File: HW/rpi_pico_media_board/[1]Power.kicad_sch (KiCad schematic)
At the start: 30 parts, among them IC1 LS1205EVD33, Q1 T2N7002AK, U3 HT7533-1

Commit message: Scheme improvements
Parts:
- renumbered C1 to C100, C2 to C101, C3 to C102, C4 to C103, C5 to C104, C6 to C105, C7 to C106, C8 to C107, C9 to C108, C10 to C109, C11 to C110, D1 to D100, D2 to D101, IC1 to IC100, J1 to J100, L1 to L100, PS1 to PS100, Q1 to Q100, R1 to R100, R2 to R101, R3 to R102, R4 to R103, R6 to R104, R5 to R105, R7 to R106, R8 to R107, R11 to R108, R9 to R109, R10 to R110, U3 to U100
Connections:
- net GND: now also IC100.11 (GND)
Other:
- moved on the sheet: D101, Q100, R109, R110

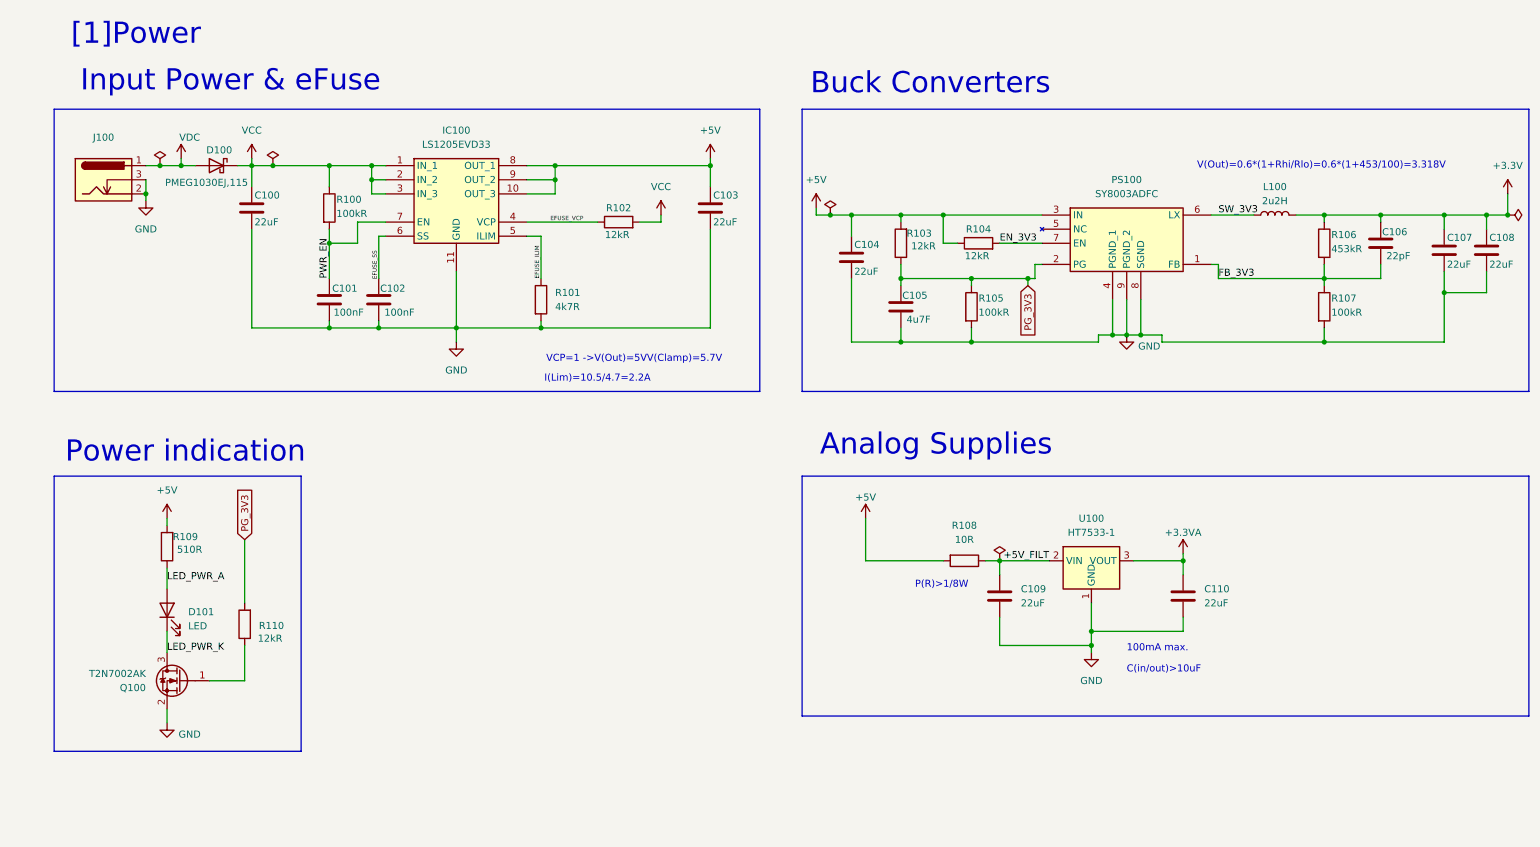
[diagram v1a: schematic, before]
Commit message: Minor BOM updates
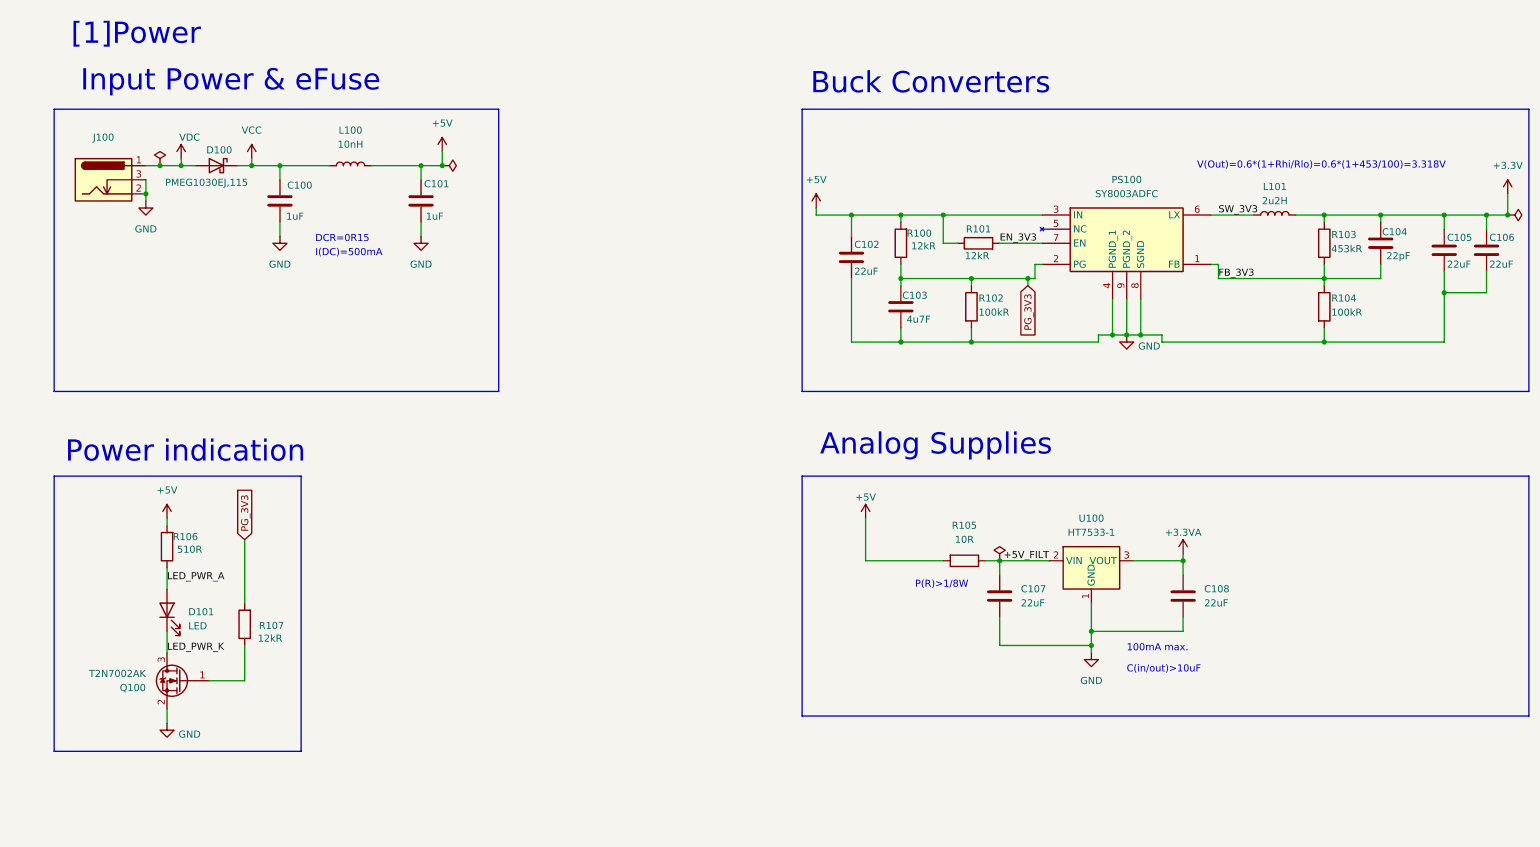
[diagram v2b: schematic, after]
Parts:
- removed C102: 100nF, Capacitor_SMD:C_0402_1005Metric, symbol Device:C
- removed C103: 22uF, Capacitor_SMD:C_1206_3216Metric, symbol Device:C
- removed IC100: LS1205EVD33, rpi_pico_media_board_power:LS1205EVD33, symbol rpi_pico_media_board_power:LS1205EVD33
- removed R100: 100kR, Resistor_SMD:R_0402_1005Metric, symbol Device:R
- removed R101: 4k7R, Resistor_SMD:R_0402_1005Metric, symbol Device:R
- removed R102: 12kR, Resistor_SMD:R_0402_1005Metric, symbol Device:R
- added L100: 10nH, Inductor_SMD:L_0603_1608Metric, symbol Device:L
- C100: value 22uF -> 1uF; footprint Capacitor_SMD:C_1206_3216Metric -> Capacitor_SMD:C_0603_1608Metric; Manufacturer (none) -> Samsung Electro-Mechanics; Manufacturer Product Number (none) -> CL10A105KB8NNNC; Manufacturer_Name Samwha Capacitor -> (none); Manufacturer_Part_Number CS3216X5R226M160NRI -> (none)
- C101: value 100nF -> 1uF; footprint Capacitor_SMD:C_0402_1005Metric -> Capacitor_SMD:C_0603_1608Metric; Manufacturer (none) -> Samsung Electro-Mechanics; Manufacturer Product Number (none) -> CL10A105KB8NNNC; Manufacturer_Name Samwha Capacitor -> (none); Manufacturer_Part_Number CS1005X7R104K500NR -> (none)
- C102: renamed from C104; Manufacturer (none) -> Samwha Capacitor; Manufacturer Part Number (none) -> CS3216X5R226M160NRI; Manufacturer_Name Samwha Capacitor -> (none); Manufacturer_Part_Number CS3216X5R226M160NRI -> (none)
- C103: renamed from C105; Manufacturer (none) -> Samsung Electro-Mechanics; Manufacturer Part Number (none) -> CL10A475KP8NNNC; Manufacturer_Name Samsung Electro-Mechanics -> (none); Manufacturer_Part_Number CL10A475KP8NNNC -> (none)
- C104: renamed from C106; footprint Capacitor_SMD:C_0402_1005Metric -> Capacitor_SMD:C_0603_1608Metric; Manufacturer (none) -> Samsung Electro-Mechanics; Manufacturer Part Number (none) -> CL10C220JB8NNNC; Manufacturer_Name YAGEO -> (none); Manufacturer_Part_Number CC0402GRNPO9BN220 -> (none)
- C105: renamed from C107; Manufacturer (none) -> Samwha Capacitor; Manufacturer Part Number (none) -> CS3216X5R226M160NRI; Manufacturer_Name Samwha Capacitor -> (none); Manufacturer_Part_Number CS3216X5R226M160NRI -> (none)
- C106: renamed from C108; Manufacturer (none) -> Samwha Capacitor; Manufacturer Part Number (none) -> CS3216X5R226M160NRI; Manufacturer_Name Samwha Capacitor -> (none); Manufacturer_Part_Number CS3216X5R226M160NRI -> (none)
- C107: renamed from C109; footprint Capacitor_SMD:C_0603_1608Metric -> Capacitor_SMD:C_1206_3216Metric; Manufacturer Samsung Electro-Mechanics -> Samwha Capacitor; Manufacturer Part Number CL10A226MP8NUNE -> CS3216X5R226M160NRI
- C108: renamed from C110; footprint Capacitor_SMD:C_0603_1608Metric -> Capacitor_SMD:C_1206_3216Metric; Manufacturer Samsung Electro-Mechanics -> Samwha Capacitor; Manufacturer Part Number CL10A226MP8NUNE -> CS3216X5R226M160NRI
- D100: Manufacturer (none) -> Nexperia; Manufacturer Part Number (none) -> PMEG1030EJ,115; Manufacturer_Name Nexperia -> (none); Manufacturer_Part_Number PMEG1030EJ,115 -> (none)
- D101: Manufacturer (none) -> XINGLIGHT; Manufacturer Part Number (none) -> XL-1608SURC-06; Manufacturer_Name XINGLIGHT -> (none); Manufacturer_Part_Number XL-1608SURC-06 -> (none)
- L101: renamed from L100; Manufacturer (none) -> Murata Electronics; Manufacturer Part Number (none) -> LQM2HPN2R2MG0L; Manufacturer_Name Murata Electronics -> (none); Manufacturer_Part_Number LQM2HPN2R2MG0L -> (none)
- PS100: Manufacturer (none) -> Silergy; Manufacturer Part Number (none) -> SY8003ADFC; Manufacturer_Name Silergy -> (none); Manufacturer_Part_Number SY8003ADFC -> (none)
- Q100: Manufacturer (none) -> TOSHIBA; Manufacturer Part Number (none) -> T2N7002AK,LM; Manufacturer_Name TOSHIBA -> (none); Manufacturer_Part_Number T2N7002AK,LM -> (none)
- renumbered R103 to R100, R104 to R101, R105 to R102, R106 to R103, R107 to R104, R108 to R105, R109 to R106, R110 to R107
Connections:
- net PWR_EN is gone; now on net +5V: C101.1
- net +5V: now also L100.2
- net VCC: now also L100.1
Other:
- note added: "DCR=0R15"
- note added: "I(DC)=500mA"
- note removed: "I(Lim)=10.5/4.7=2.2A"
- note removed: "VCP=1 ->V(Out)=5VV(Clamp)=5.7V"

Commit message: DRC cleanup
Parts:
- removed J100: ~, Connector_BarrelJack:BarrelJack_GCT_DCJ200-10-A_Horizontal, symbol ZettBrettPower:BarrelJack
- added J1: Barrel_Jack_Switch_Pin3Ring, Connector_BarrelJack:BarrelJack_GCT_DCJ200-10-A_Horizontal, symbol Connector:Barrel_Jack_Switch_Pin3Ring
- C100, C101: Manufacturer Part Number (none) -> CL10A105KB8NNNC; Manufacturer Product Number CL10A105KB8NNNC -> (none)
- R100, R101, R107: footprint Resistor_SMD:R_0402_1005Metric -> Resistor_SMD:R_0603_1608Metric; Manufacturer (none) -> UNI-ROYAL(Uniroyal Elec); Manufacturer Part Number (none) -> 0603WAF1202T5E; Manufacturer_Name UNI-ROYAL(Uniroyal Elec) -> (none); Manufacturer_Part_Number 0402WGF1202TCE -> (none)
- R102, R104: footprint Resistor_SMD:R_0402_1005Metric -> Resistor_SMD:R_0603_1608Metric; Manufacturer (none) -> UNI-ROYAL(Uniroyal Elec); Manufacturer Part Number (none) -> 0603WAF1003T5E; Manufacturer_Name UNI-ROYAL(Uniroyal Elec) -> (none); Manufacturer_Part_Number 0402WGF1003TCE -> (none)
- R103: footprint Resistor_SMD:R_0402_1005Metric -> Resistor_SMD:R_0603_1608Metric; Manufacturer (none) -> UNI-ROYAL(Uniroyal Elec); Manufacturer Part Number (none) -> 0603WAF4533T5E; Manufacturer_Name UNI-ROYAL(Uniroyal Elec) -> (none); Manufacturer_Part_Number 0402WGF4533TCE -> (none)
- R106: footprint Resistor_SMD:R_0402_1005Metric -> Resistor_SMD:R_0603_1608Metric; Manufacturer (none) -> UNI-ROYAL(Uniroyal Elec); Manufacturer Part Number (none) -> 0603WAF5100T5E; Manufacturer_Name UNI-ROYAL(Uniroyal Elec) -> (none); Manufacturer_Part_Number 0402WGF5100TCE -> (none)
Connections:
- net GND: now also J1.2, J1.3
- net VDC: now also J1.1

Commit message: Very initial PCB layout
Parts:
- added C109, C110: 22uF, Capacitor_SMD:C_1206_3216Metric, symbol Device:C
- added R106: 10R, Resistor_SMD:R_0805_2012Metric, symbol Device:R
- added U101: HT7533-1, Package_TO_SOT_SMD:SOT-89-3, symbol Regulator_Linear:HT75xx-1-SOT89
- renumbered R106 to R107, R107 to R108
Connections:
- net +5V: now also R106.2
- net GND: now also C109.2, C110.2, U101.1 (GND)
- net +3.3VA renamed +3.3VA_PCM
- net +5V_FILT renamed +5V_FILT_1
- new net +3.3VA_INMP: C110.1, U101.3 (VOUT)
- new net +5V_FILT_2: C109.1, R106.1, U101.2 (VIN)
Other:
- moved on the sheet: C107, C108, R105, U100

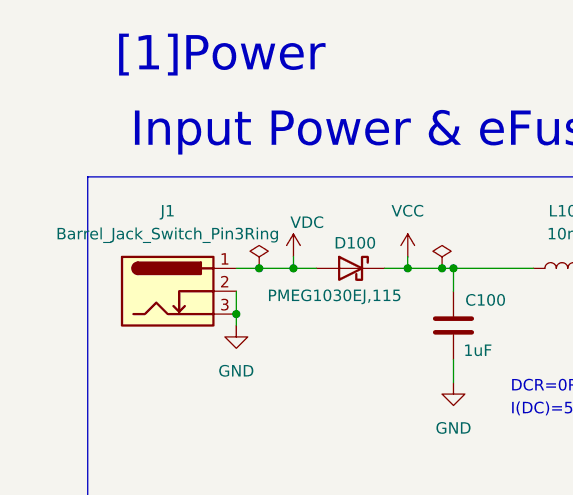
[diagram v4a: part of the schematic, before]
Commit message: SD Card routing
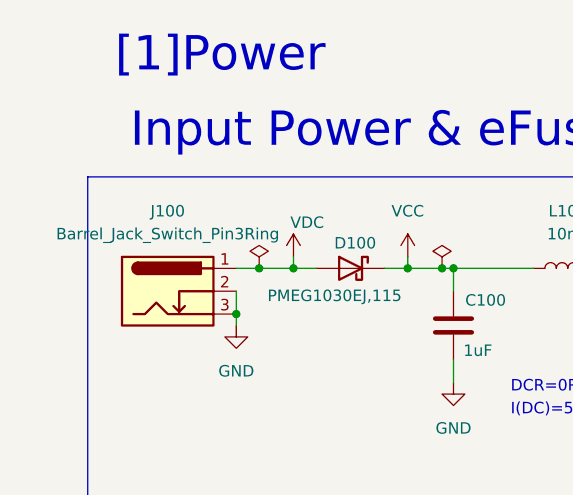
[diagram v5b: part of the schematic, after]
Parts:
- renumbered J1 to J100
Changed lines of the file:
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@@
 		(dnp no)
 		(fields_autoplaced yes)
-		(property "Reference" "J1"
+		(property "Reference" "J100"
 			(at 22.86 34.29 0)
 			(effects
@@
 			(project ""
 				(path "/883c739e-d2a5-4bc8-a050-29a6043b4072/1577bc80-f712-4867-9ef7-56f611800069"
-					(reference "J1")
+					(reference "J100")
 					(unit 1)
 				)
